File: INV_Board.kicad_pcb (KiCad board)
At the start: 4 copper layers, 84 x 66.5 mm, 188 parts, among them J1 USB_B_Micro, J10 Conn_01x02_Male, J11 Conn_01x04_Male, J12 Conn_01x06_Female, J2 Conn_01x02_Male, J3 Conn_01x02_Male, J4 Conn_01x02_Male, J6 Conn_01x08_Female, J7 Conn_01x03_Male, J8 Conn_ARM_JTAG_SWD_10, J9 Conn_01x06_Male, Q1 Q_NMOS_GDS, Q10 IPT015N10N5, Q11 IPT015N10N5, Q12 IPT015N10N5, Q2 Q_NMOS_GDS, Q3 Q_NMOS_GDS, Q4 Q_NMOS_GDS, Q5 Q_NMOS_GDS, Q6 Q_NMOS_GDS, Q7 IPT015N10N5, Q8 IPT015N10N5, Q9 IPT015N10N5, U1 INA181, U10 INA181, U2 STM32F303CBTx, U3 IR2181, U4 IR2181, U5 IR2181, U6 TPS76333, U7 LM5017MR, U8 TPS61041DDC, U9 INA181, X1 ASE-xxxMHz

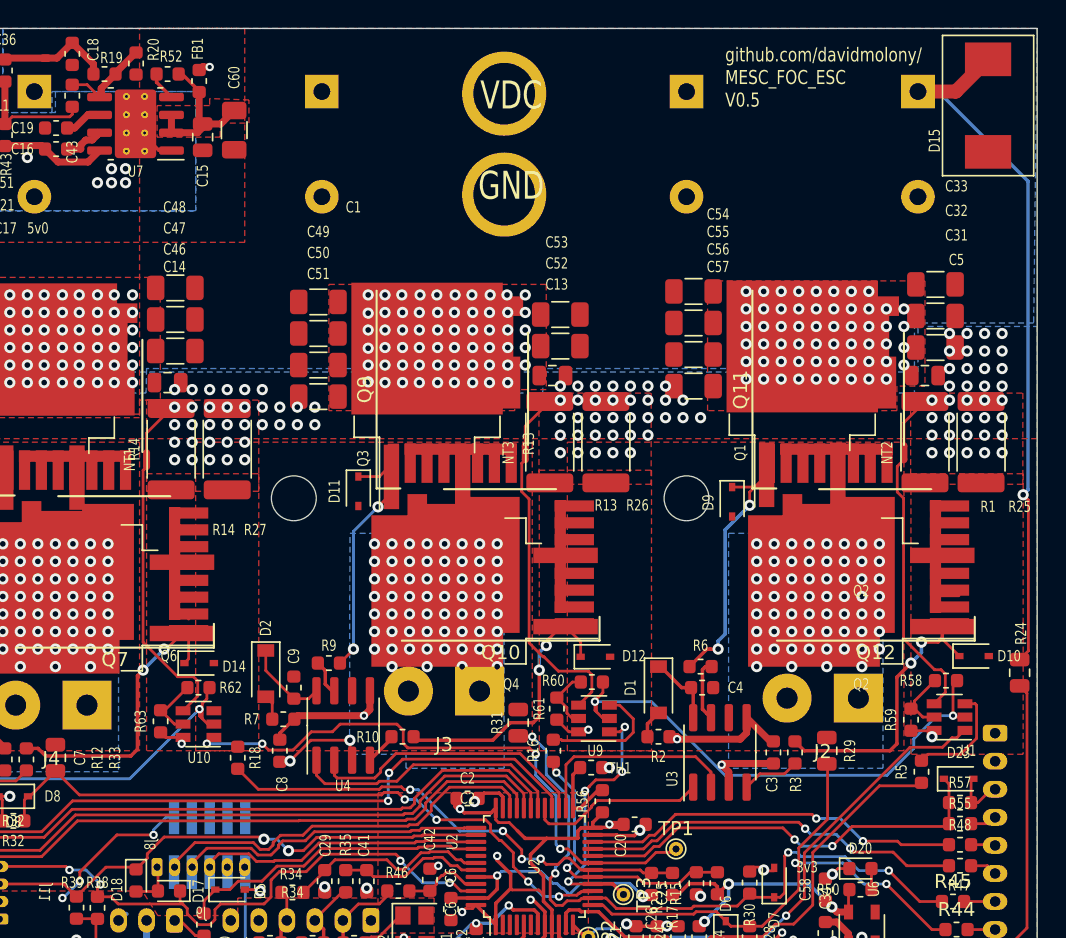
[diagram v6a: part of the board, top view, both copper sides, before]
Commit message: Add series resistors to the opamp outputs, this will protect against fighting MCU and ops. Move the Ceramic caps near the DCDC to clear possible top fit capacitors. Increase clearance for different shunt styles - avoid shunt+ and GND overlapping.
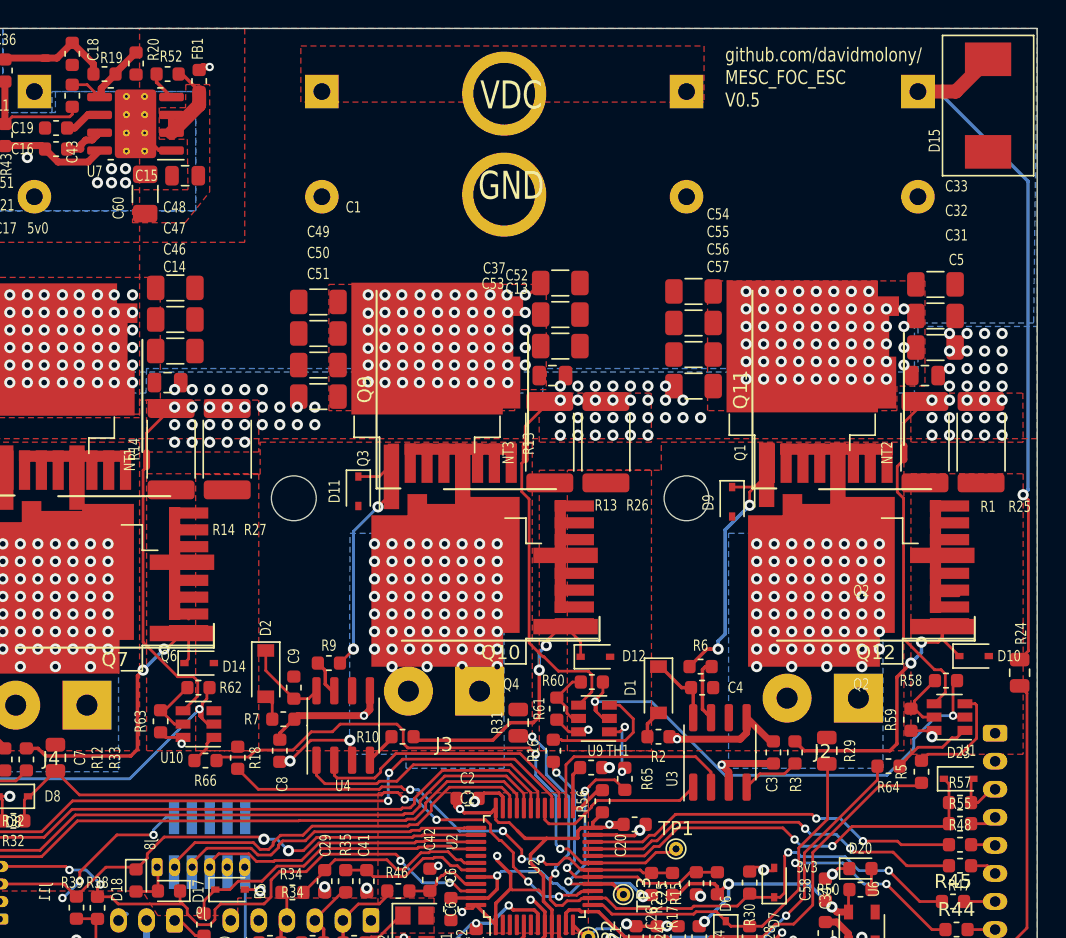
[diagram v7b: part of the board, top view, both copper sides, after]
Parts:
- added C37: C_1uF 100V, Capacitor_SMD:C_1206_3216Metric, F.Cu at (166.0, 67.2)
- added R64: R_150, Resistor_SMD:R_0603_1608Metric, F.Cu at (189.4, 101.6)
- added R65: R_150, Resistor_SMD:R_0603_1608Metric, F.Cu at (170.6, 102.5)
- added R66: R_150, Resistor_SMD:R_0603_1608Metric, F.Cu at (140.7, 101.2)
- moved C60 7.81 mm to (136.4, 60.8), turned to 270 degrees
- moved C15 3.02 mm to (139.2, 59.5), turned to 180 degrees
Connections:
- U1 pad 1: /op1Vout -> Net-(R64-Pad2)
- U10 pad 1: /op3Vout -> Net-(R66-Pad2)
- U9 pad 1: /op2Vout -> Net-(R65-Pad2)
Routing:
- net /op1Vout: track 36.9 -> 30.0 mm
- net Net-(R64-Pad2): track 0.00 -> 5.89 mm
- net Net-(R65-Pad2): track 0.00 -> 4.53 mm, vias 0 -> 2
- net Net-(C15-Pad1): track 11.5 -> 7.23 mm
- net /op2Vout: track 19.2 -> 14.9 mm, vias 4 -> 2
- net Net-(R66-Pad2): track 0.00 -> 2.25 mm
- net +VDC: track 51.6 -> 53.1 mm
- net /op3Vout: track 43.1 -> 41.8 mm, vias 4 -> 2
- net GND: vias 158 -> 143

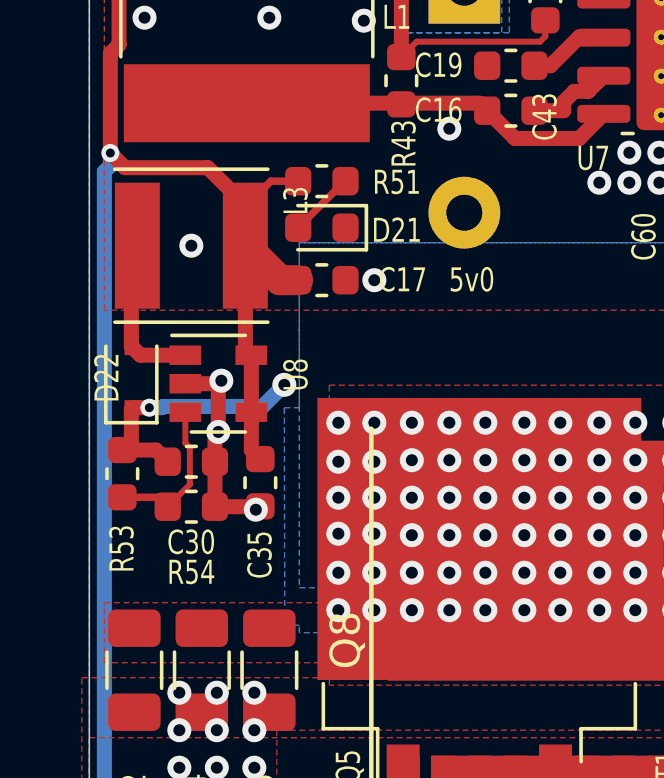
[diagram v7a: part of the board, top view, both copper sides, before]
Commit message: Optimise layout of DCDC boost to eliminate inducive loop on DCDC, hopefully eliminate ringing.
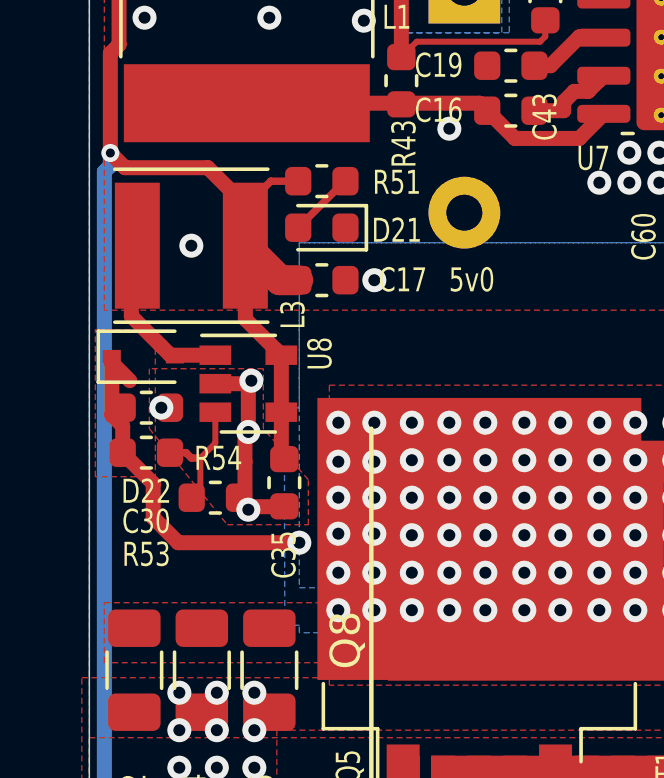
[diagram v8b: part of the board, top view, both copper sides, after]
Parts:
- moved C30 2.34 mm to (117.9, 67.5)
- moved R53 1.06 mm to (117.9, 69.0), turned to 180 degrees
- moved U8 1.00 mm to (121.3, 66.7)
- moved R54 0.85 mm to (120.2, 70.5)
- moved D22 0.81 mm to (117.8, 65.8), turned to 0 degrees
- moved C35 0.80 mm to (122.5, 70.0)
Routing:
- net +12V: track 126.0 -> 129.7 mm, vias 5 -> 4
- net +5V: track 128.7 -> 129.4 mm
- net GND: vias 143 -> 144
- added copper zone on F.Cu, net +12V
